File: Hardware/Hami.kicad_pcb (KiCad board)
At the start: 2 copper layers, 77.5 x 117.5 mm, 50 parts, among them J1 OLED, J2 BAT, SW1 Reset, SW10 MX, SW11 MX, SW12 MX, SW13 MX, SW14 MX, SW15 MX, SW16 MX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

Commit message: Added renders and updated readme
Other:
- board text removed: "JLCJLCJLC"

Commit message: Changed footprint references
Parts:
- J1: footprint Numpad:PinHeader_1x04_P2.54mm_Vertical_No_Silk -> Hami:PinHeader_1x04_P2.54mm_Vertical_No_Silk
- J2: footprint Numpad:Battery_Solder_Points -> Hami:Battery_Solder_Points
- SW10, SW11, SW12, SW13, SW14, SW15, SW16, SW17, SW2, SW3, SW4, SW5, SW6, SW7, SW8, SW9: footprint Numpad:CherryMX_Hotswap_SMK -> Hami:CherryMX_Hotswap_SMK
- SW18, SW19: footprint Numpad:CherryMX_Hotswap_2u_SMK -> Hami:CherryMX_Hotswap_2u_SMK
- U1: footprint Numpad:ArduinoProMicro_Blank -> Hami:ArduinoProMicro_Blank

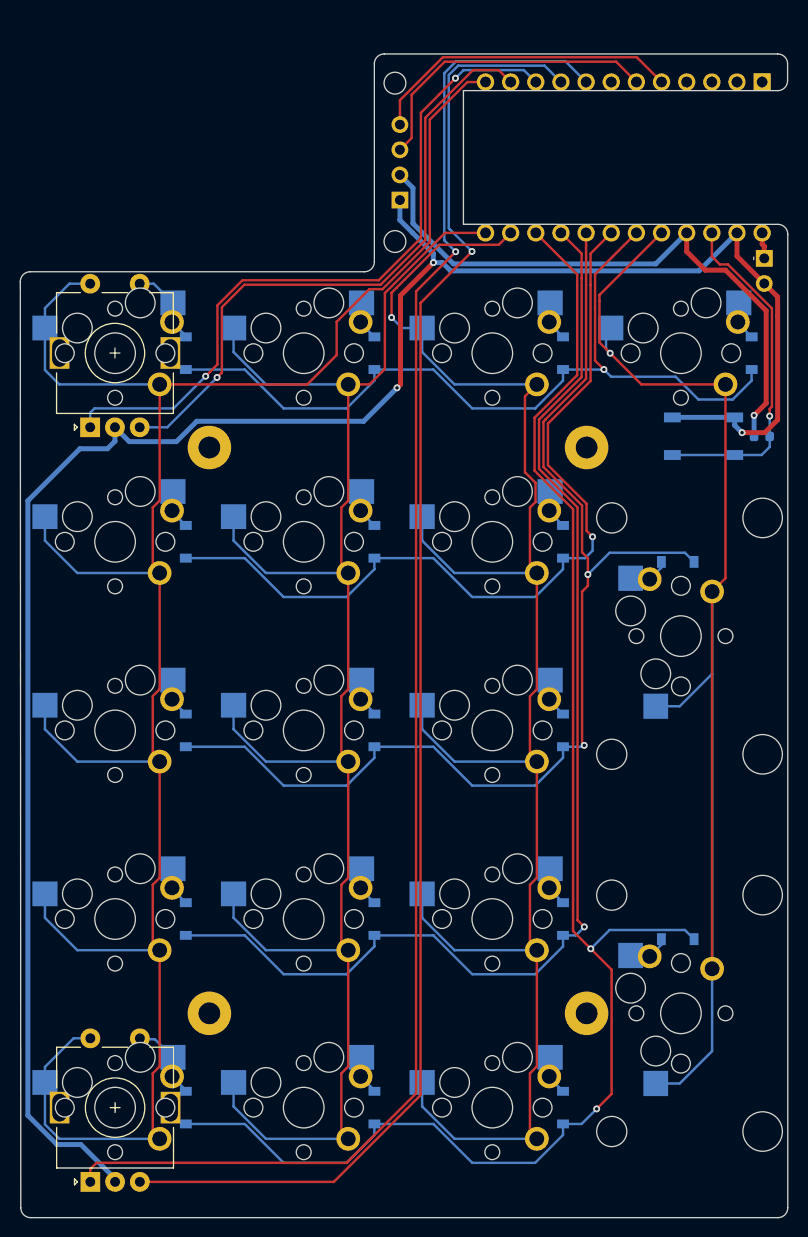
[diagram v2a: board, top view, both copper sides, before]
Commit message: Moved position of OLED, added new plate
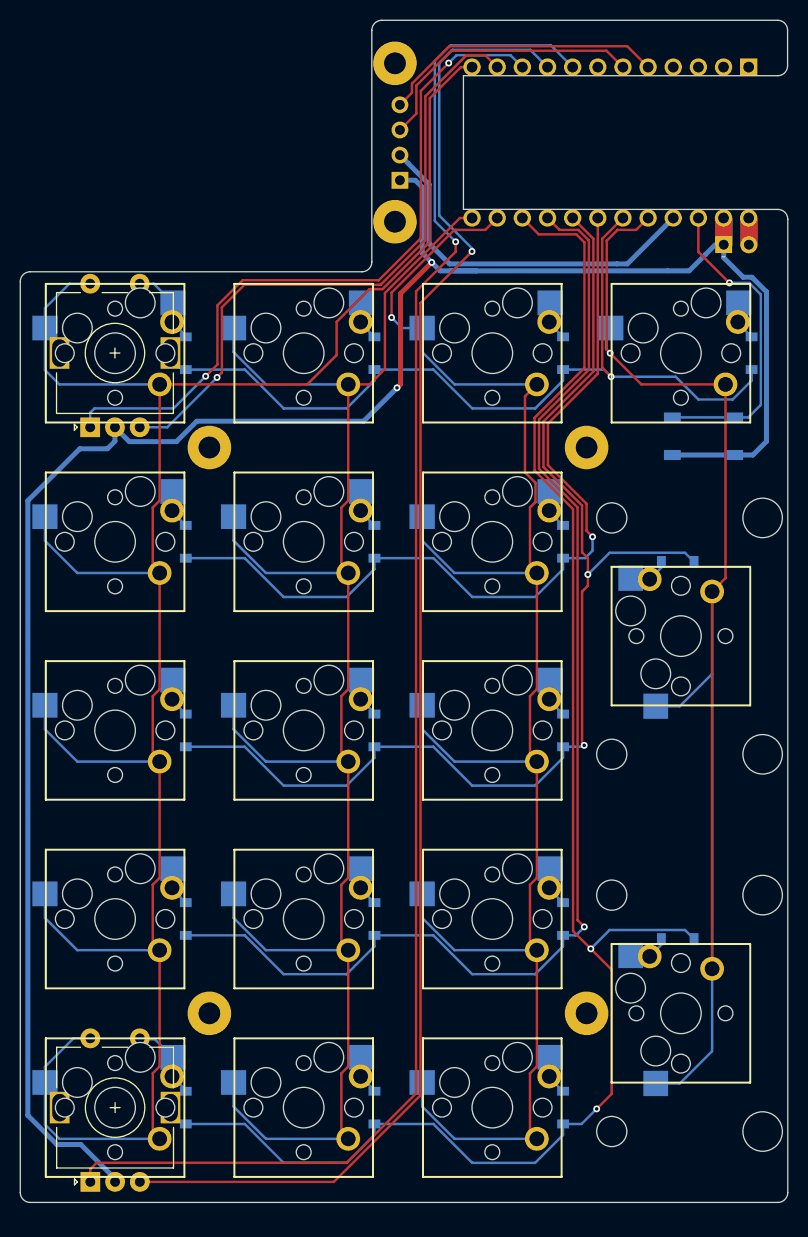
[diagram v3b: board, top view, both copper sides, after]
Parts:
- removed R1: R_Small, Resistor_SMD:R_0603_1608Metric
- REF** (x2): value MountingHole_2.2mm_M2 -> MountingHole_2.2mm_M2_Pad; footprint MountingHole:MountingHole_2.2mm_M2 -> MountingHole:MountingHole_2.2mm_M2_Pad
- moved J2 4.32 mm to (178.9, 52.5), turned to 90 degrees
- moved U1 2.03 mm to (167.5, 42.2)
- moved J1 2.00 mm to (146.2, 42.2)
- moved REF** 2.00 mm to (145.7, 34.2)
- moved REF** 2.00 mm to (145.7, 50.2)
- moved G*** 0.40 mm to (174.2, 107.2)
- turned SW1 to 180 degrees
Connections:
- J2 pad 1: Net-(J2-Pad1) -> GND
- J2 pad 2: GND -> Net-(J2-Pad2)
- U1 pad 24: Net-(J2-Pad1) -> Net-(J2-Pad2)
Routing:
- net VCC: track 61.7 -> 37.6 mm, vias 1 -> 0
- net GND: track 205.2 -> 212.5 mm, vias 3 -> 2
- net Net-(J2-Pad2): track 0.00 -> 4.97 mm
- net ROW5: track 157.4 -> 162.3 mm
- net ROW4: track 123.1 -> 126.8 mm
- net SDA: track 31.7 -> 28.9 mm
- net SCL: track 31.0 -> 28.2 mm
- net RESET: track 34.9 -> 32.1 mm
- net ROW3: track 115.9 -> 118.5 mm
- net Net-(J2-Pad1): track 2.66 -> 0.00 mm
- net COL4: track 150.9 -> 152.4 mm
- net Rot_2A: track 158.2 -> 159.6 mm
- net Rot_2B: track 150.6 -> 152.0 mm
- net ROW1: track 84.0 -> 85.4 mm
- net ROW2: track 85.8 -> 86.8 mm
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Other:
- board size 77.5 x 117.5 mm -> 77.5 x 119.4 mm
- board text added: "Hami V1.1 Aria"
- board text removed: "Hami V1.1 Designed by Aria"
